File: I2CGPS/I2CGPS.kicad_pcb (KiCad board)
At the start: 2 copper layers, 5 parts, among them P1 CONN_01X05, U1 GY-NEO6MV2

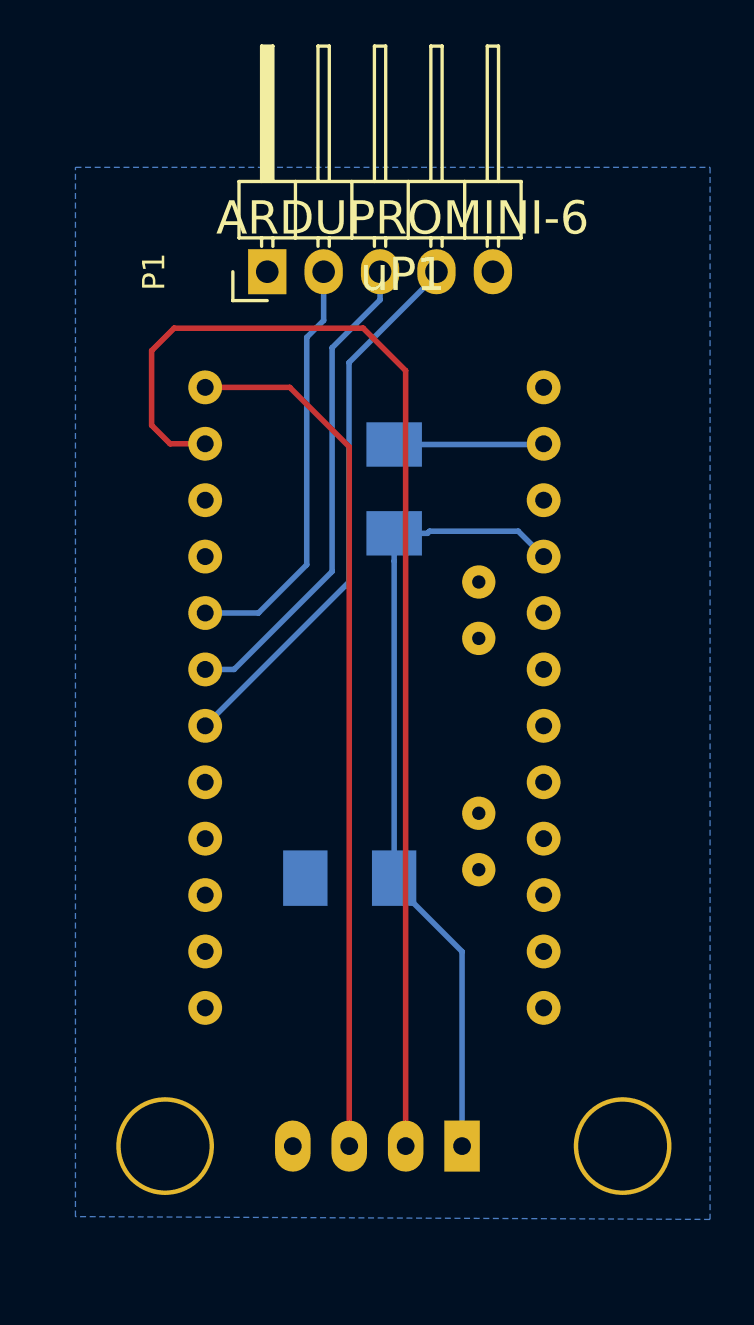
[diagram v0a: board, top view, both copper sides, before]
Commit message: IC2 GPS with power down fet
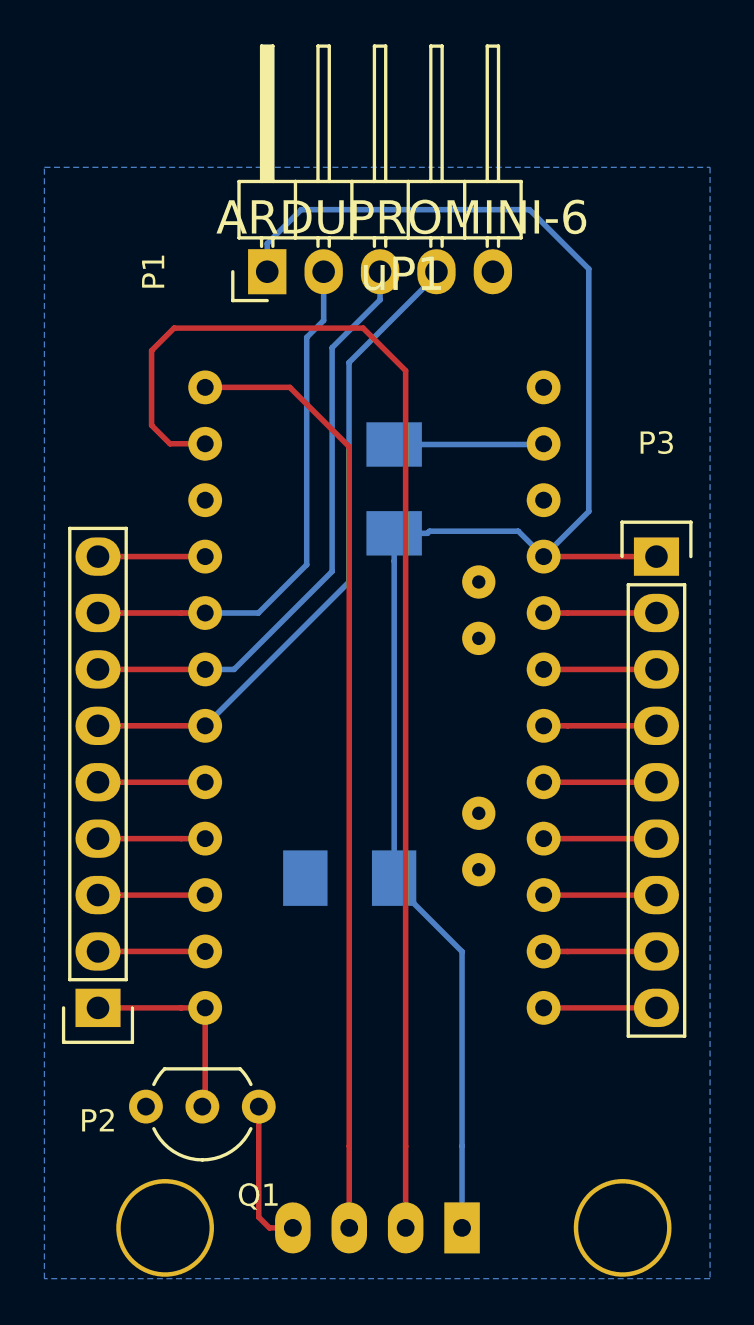
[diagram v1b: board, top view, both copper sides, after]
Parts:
- added P2: CONN_01X09, Pin_Headers:Pin_Header_Straight_1x09, F.Cu at (184.8, 114.8)
- added P3: CONN_01X09, Pin_Headers:Pin_Header_Straight_1x09, F.Cu at (209.9, 94.5)
- added Q1: BS170, TO_SOT_Packages_THT:TO-92_Inline_Wide, F.Cu at (192.0, 119.3)
- moved U1 3.68 mm to (210.6, 126.9)
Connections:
- U1 pad 4: GND -> Net-(Q1-Pad1)
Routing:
- net VCC: track 36.1 -> 76.1 mm
- net Net-(P2-Pad1): track 0.00 -> 9.50 mm
- net Net-(Q1-Pad1): track 0.00 -> 6.71 mm
- net Net-(P3-Pad9): track 0.00 -> 5.08 mm
- net Net-(P3-Pad8): track 0.00 -> 5.08 mm
- net Net-(P3-Pad7): track 0.00 -> 5.08 mm
- net Net-(P3-Pad6): track 0.00 -> 5.08 mm
- net Net-(P3-Pad5): track 0.00 -> 5.08 mm
- net Net-(P3-Pad4): track 0.00 -> 5.08 mm
- net Net-(P3-Pad3): track 0.00 -> 5.08 mm
- net Net-(P3-Pad2): track 0.00 -> 5.08 mm
- net SDA: track 19.0 -> 23.8 mm
- net SCL: track 21.9 -> 26.8 mm
- net Net-(P2-Pad5): track 0.00 -> 4.83 mm
- net Net-(P2-Pad4): track 0.00 -> 4.83 mm
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
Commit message: resized to particle sensor and panelized
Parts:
- added R1: R, Resistors_SMD:R_1210_HandSoldering, B.Cu at (207.5, 118.9)
- Q1: value BS170 -> BSS84; footprint TO_SOT_Packages_THT:TO-92_Inline_Wide -> TO_SOT_Packages_SMD:SOT-23; moved to B.Cu
- moved Q1 8.09 mm to (200.1, 118.8), turned to 270 degrees
- moved P1 0.89 mm to (192.4, 82.5)
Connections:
- P3 pad 1: VCC -> Net-(P3-Pad1)
- Q1 pad 1: Net-(Q1-Pad1) -> Net-(P3-Pad9)
- Q1 pad 2: Net-(P2-Pad1) -> Net-(Q1-Pad2)
- Q1 pad 3: GND -> VCC
- U1 pad 1: VCC -> Net-(Q1-Pad2)
- U1 pad 4: Net-(Q1-Pad1) -> GND
- uP1 pad 19: Net-(uP1-Pad19) -> VCC
- uP1 pad 22: VCC -> Net-(P3-Pad1)
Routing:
- net VCC: track 76.1 -> 64.9 mm
- net Net-(P3-Pad9): track 5.08 -> 14.2 mm
- net Net-(Q1-Pad1): track 6.71 -> 0.00 mm
- net GND: track 11.6 -> 4.87 mm
- net Net-(Q1-Pad2): track 0.00 -> 5.57 mm
- net Net-(P3-Pad1): track 0.00 -> 5.08 mm
- net RX: track 57.4 -> 52.4 mm
- net Net-(P2-Pad1): track 9.50 -> 4.83 mm
- net SDA: track 23.8 -> 22.3 mm
- net TX: track 42.8 -> 41.4 mm
- net SCL: track 26.8 -> 25.9 mm
- added copper zone on F.Cu, net GND

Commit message: added adem logo's
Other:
- board outline added: 29 x 49 mm
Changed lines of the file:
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@@
     (links 36)
     (no_connects 0)
-    (area 0 0 0 0)
+    (area 179.751667 71.674999 223.879562 134.400001)
     (thickness 1.6)
-    (drawings 6)
+    (drawings 10)
     (tracks 92)
     (zones 0)
@@
       (drillshape 1)
       (scaleselection 1)
-      (outputdirectory ""))
+      (outputdirectory ../))
   )
   (net 0 "")
@@
     )
   )
+  (gr_line (start 183 127) (end 183 78) (layer Edge.Cuts) (width 0.15))
+  (gr_line (start 212 127) (end 183 127) (layer Edge.Cuts) (width 0.15))
+  (gr_line (start 212 78) (end 212 127) (layer Edge.Cuts) (width 0.15))
+  (gr_line (start 183 78) (end 212 78) (layer Edge.Cuts) (width 0.15))
   (dimension 49 (width 0.3) (layer Eco2.User)
     (gr_text 49.000mm (at 217.95099 102.5 90) (layer Eco2.User)

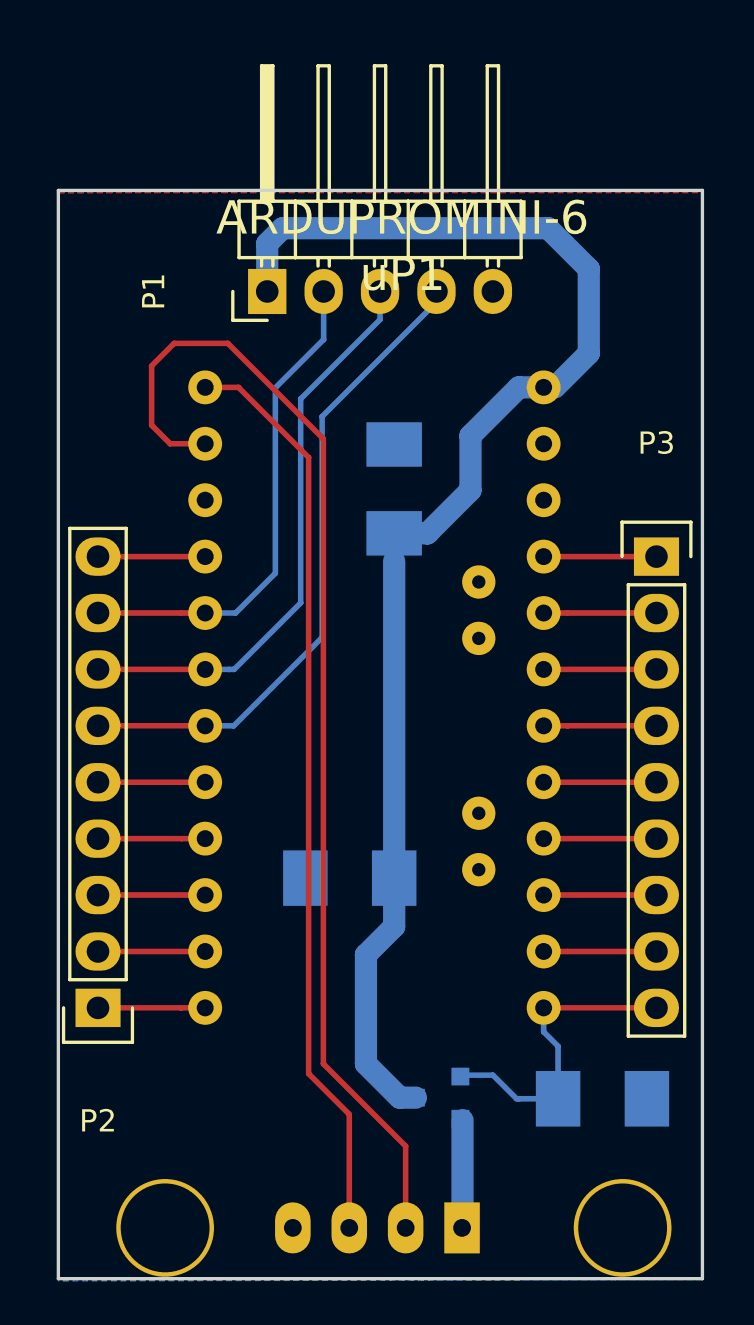
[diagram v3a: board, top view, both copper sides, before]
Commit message: added softserial to board
allows selection of hardware serial or soft serial by solder selector
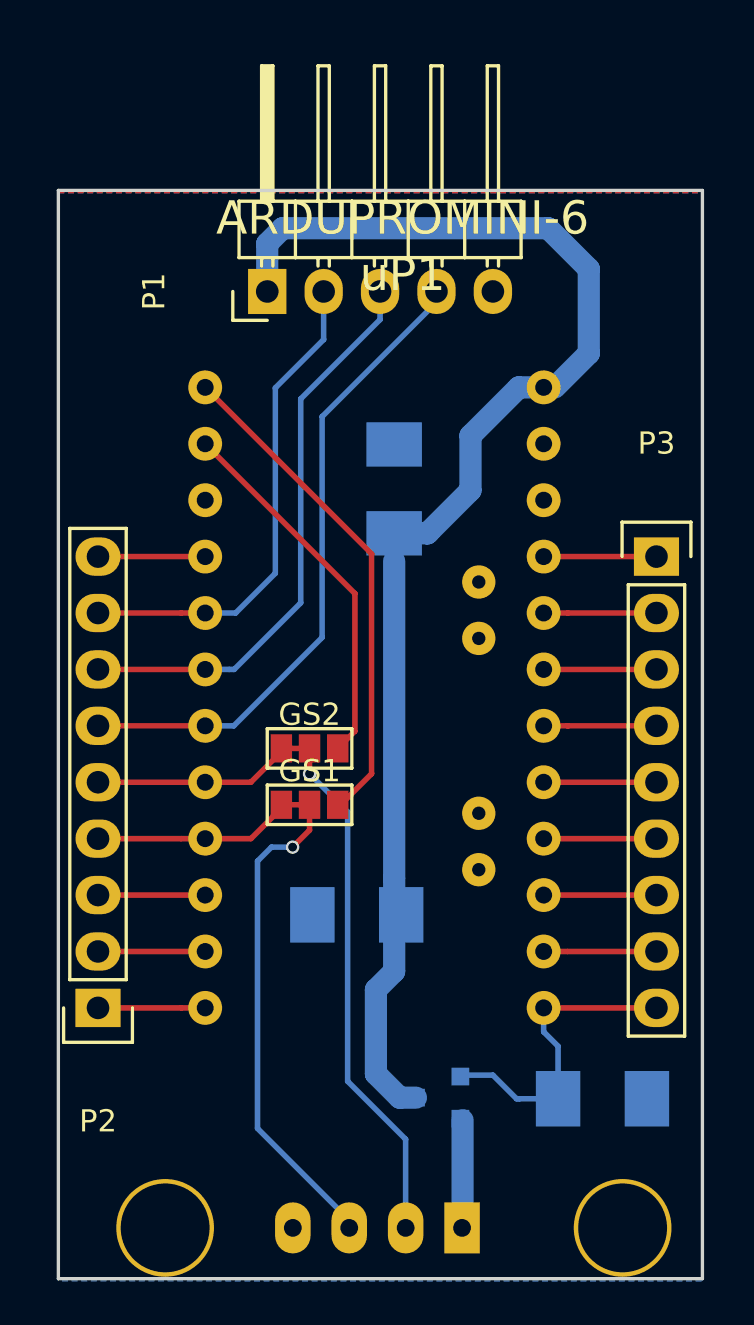
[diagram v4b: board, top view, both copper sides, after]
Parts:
- added GS1: GS3, GS3, F.Cu at (194.3, 105.7)
- added GS2: GS3, GS3, F.Cu at (194.3, 103.1)
- moved C1 1.68 mm to (196.4, 110.6)
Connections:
- P2 pad 4: Net-(P2-Pad4) -> TX
- P2 pad 5: Net-(P2-Pad5) -> RX
- uP1 pad 14: Net-(P2-Pad5) -> RX
- uP1 pad 15: Net-(P2-Pad4) -> TX
- uP1 pad 7: TX -> TX_HW
- uP1 pad 8: RX -> RX_HW
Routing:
- net TX_HW: track 0.00 -> 22.6 mm
- net RX: track 52.4 -> 33.8 mm, vias 0 -> 1
- net RX_HW: track 0.00 -> 16.8 mm
- net TX: track 41.4 -> 32.5 mm, vias 0 -> 1
- net Net-(P2-Pad5): track 4.83 -> 0.00 mm
- net Net-(P2-Pad4): track 4.83 -> 0.00 mm
